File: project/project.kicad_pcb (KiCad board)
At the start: 2 copper layers, 85.5 x 85.5 mm, 53 parts, among them J101 IN, J102 1x7_5.08, J103 1x7_5.08, J104 1x7_5.08, J105 FFC Connector, K1001 P6D-04P, K1101 P6D-04P, K1201 P6D-04P, K1301 P6D-04P, K1401 P6D-04P, K1501 P6D-04P, K1601 P6D-04P, K201 P6D-04P, K301 P6D-04P, K401 P6D-04P, K501 P6D-04P, K601 P6D-04P, K701 P6D-04P, K801 P6D-04P, K901 P6D-04P, U101 GX101

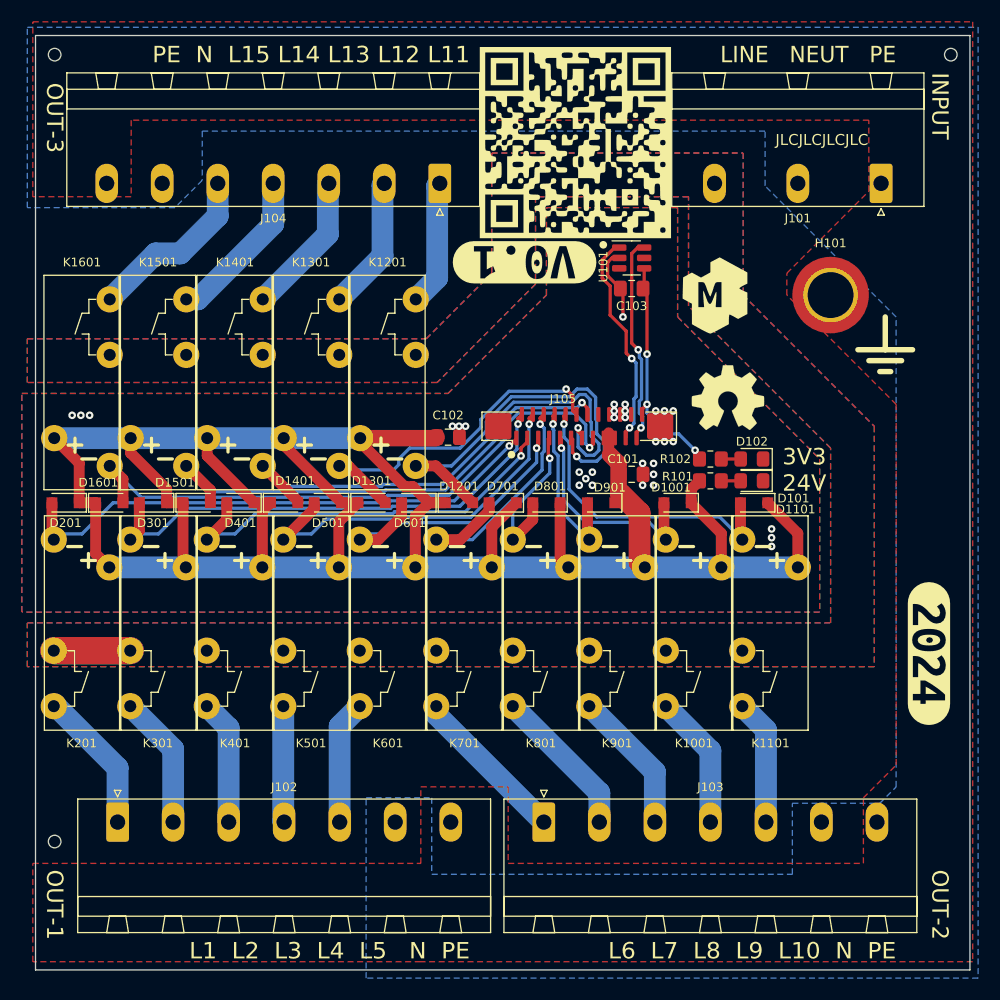
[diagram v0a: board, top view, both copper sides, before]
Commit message: pcb resize, 3d models, inset connectors, gerbers format
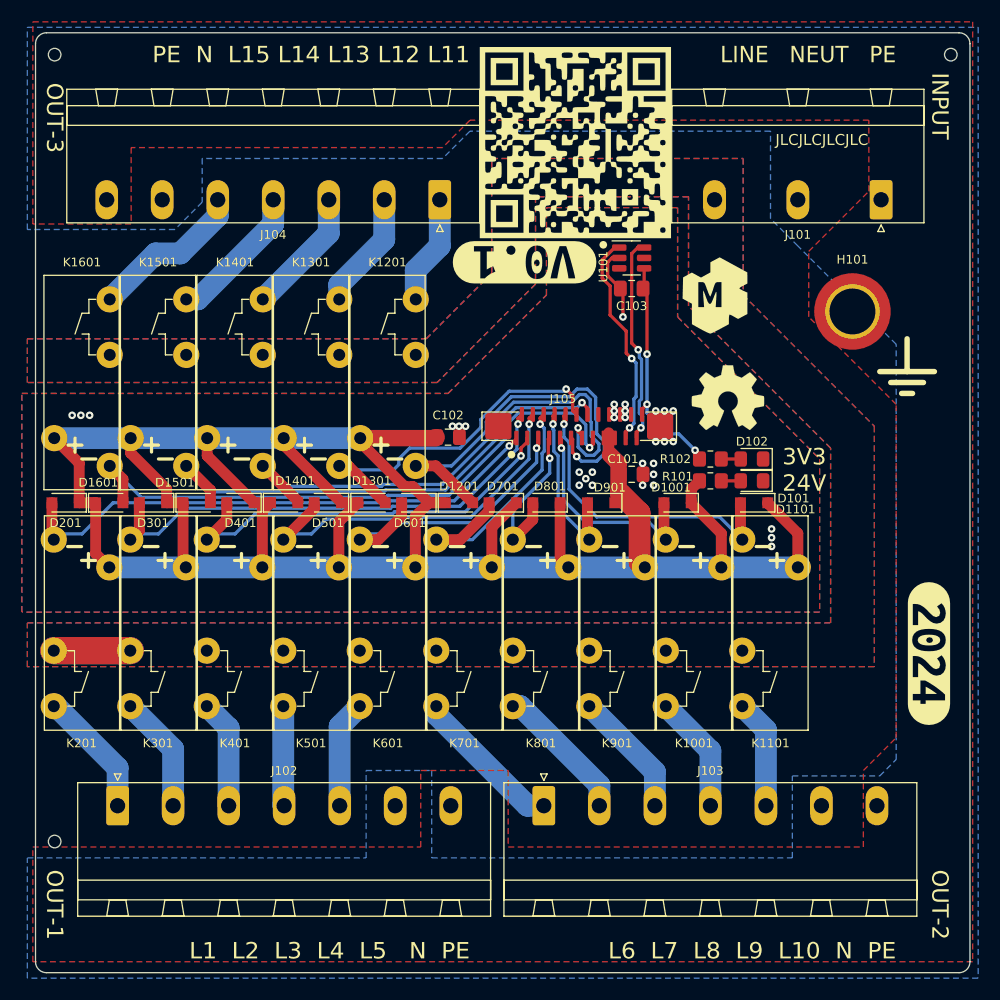
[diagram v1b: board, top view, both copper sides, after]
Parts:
- moved H101 2.50 mm to (200.3, 73.5)
- moved J101 1.50 mm to (202.9, 63.3)
- moved J102 1.50 mm to (133.0, 118.8)
- moved J103 1.50 mm to (172.0, 118.8)
- moved J104 1.50 mm to (162.5, 63.3)
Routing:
- net /_relay8/COM: track 13.9 -> 11.6 mm
- net /_relay13/COM: track 12.3 -> 10.8 mm
- net /_relay12/COM: track 11.5 -> 10.0 mm
- net /_relay9/COM: track 13.1 -> 11.6 mm
- net /_relay6/COM: track 11.4 -> 9.87 mm
- net /_relay5/COM: track 10.6 -> 9.14 mm
- net /_relay4/COM: track 11.4 -> 9.94 mm
- net /_relay3/COM: track 12.2 -> 10.7 mm
- net /_relay2/COM: track 13.1 -> 11.6 mm
- net /_relay16/COM: track 16.0 -> 14.5 mm
- net /_relay15/COM: track 14.5 -> 13.0 mm
- net /_relay11/COM: track 11.5 -> 10.0 mm
- net /_relay10/COM: track 12.3 -> 10.8 mm
- net /_relay14/COM: track 13.1 -> 11.6 mm
- net /_relay7/COM: track 14.7 -> 14.1 mm
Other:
- board size 85.5 x 85.5 mm -> 85.5 x 86 mm

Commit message: bumping up version to v0.2
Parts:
- removed kibuzzard-66DA8205: G***, kibuzzard-66DA8205
- removed kibuzzard-6750110D: G***, kibuzzard-6750110D
- added kibuzzard-6798B3BB: G***, kibuzzard-6798B3BB, F.Cu at (169.3, 69.0)
- added kibuzzard-6798B3C4: G***, kibuzzard-6798B3C4, F.Cu at (207.3, 104.8)

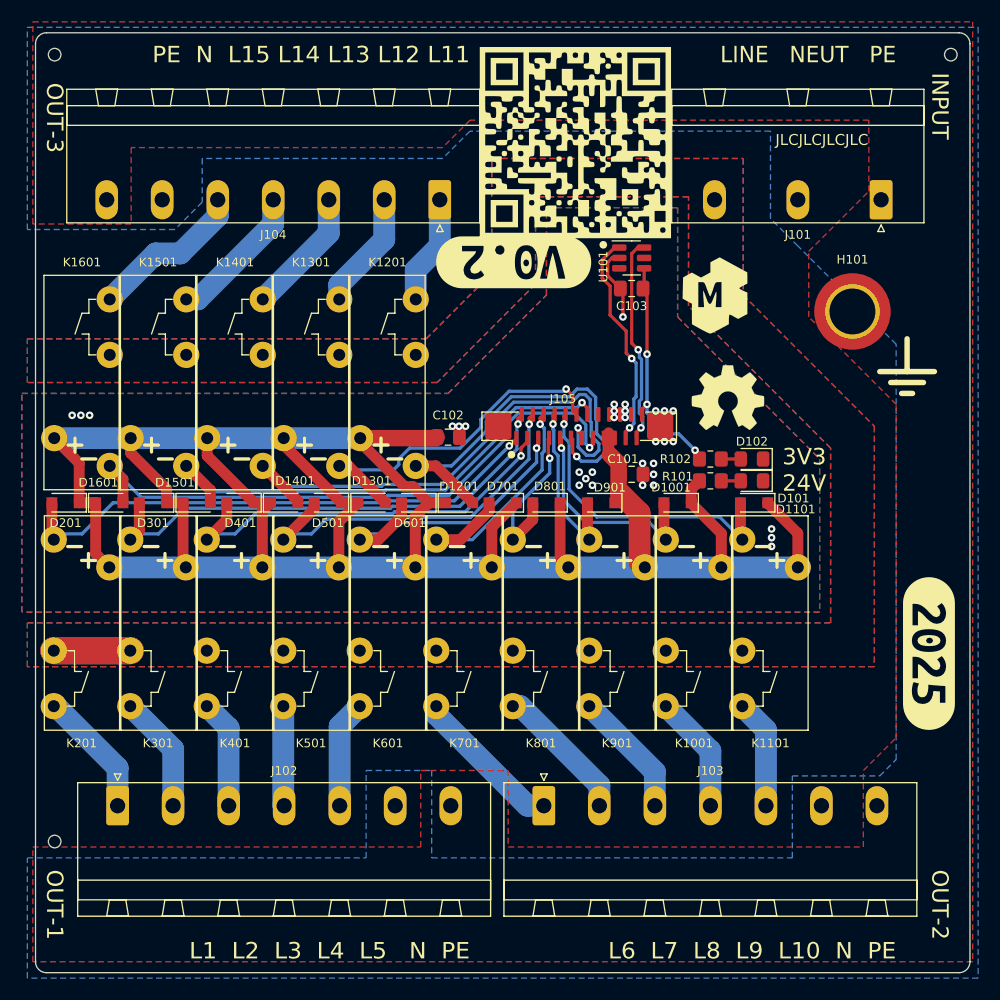
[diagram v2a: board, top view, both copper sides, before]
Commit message: replacing FFC connector
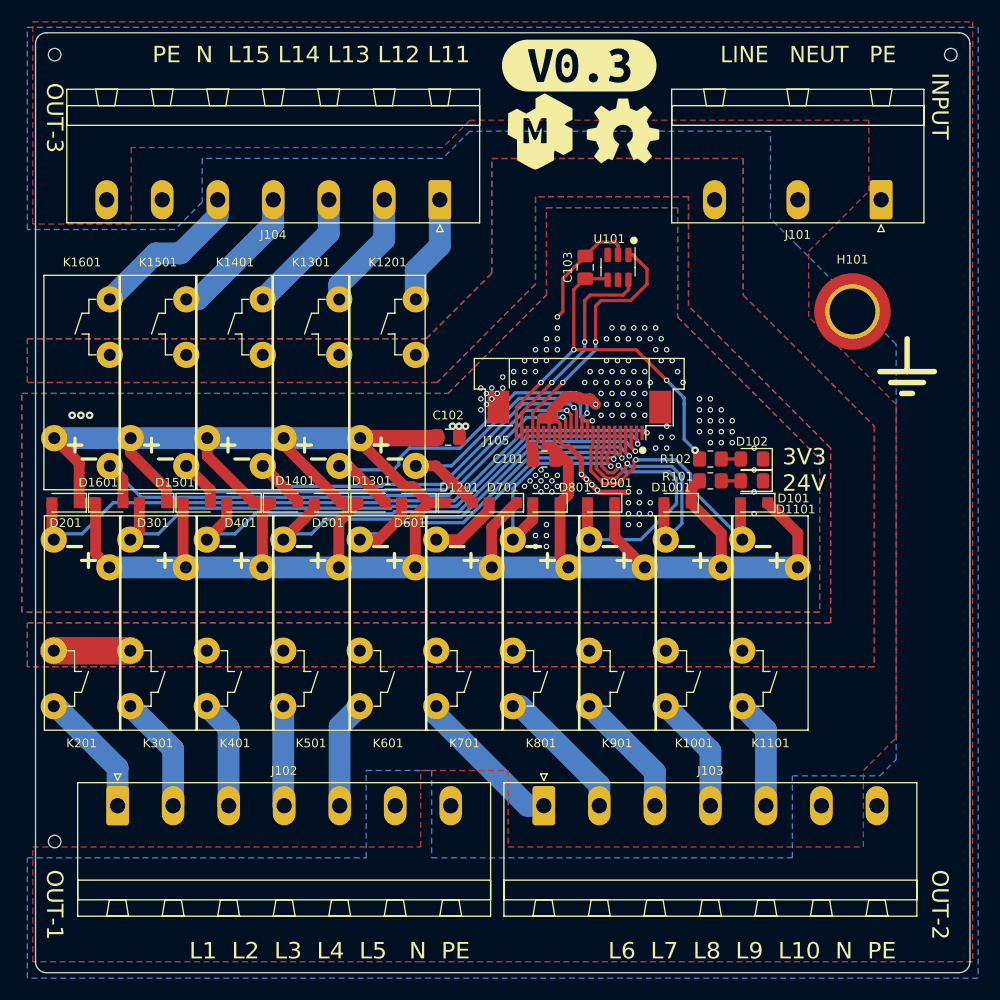
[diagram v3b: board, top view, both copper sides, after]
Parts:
- removed kibuzzard-6798B3BB: G***, kibuzzard-6798B3BB
- added kibuzzard-68EEE57B: G***, kibuzzard-68EEE57B, F.Cu at (175.3, 51.0)
- G***, kibuzzard-6798B3C4: moved to B.Cu
- J105: footprint -local:AFC11-S24ICC-00 -> -local:AFC07-S24FCC-00
- moved kibuzzard-6798B3C4 54.8 mm to (174.3, 61.0), turned to 180 degrees
- moved G*** 38.5 mm to (201.3, 86.0), turned to 180 degrees
- moved G101 26.2 mm to (179.3, 57.0)
- moved G102 21.9 mm to (171.3, 57.0)
- moved C101 8.12 mm to (172.1, 87.0), turned to 180 degrees
- moved C103 4.67 mm to (175.8, 69.5), turned to 90 degrees
- moved U101 1.52 mm to (178.8, 69.5), turned to -90 degrees
- moved J105 0.50 mm to (175.3, 83.5), turned to 180 degrees
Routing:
- net GND: track 6.81 -> 36.3 mm, vias 32 -> 136
- net +3V3: track 21.5 -> 37.1 mm, vias 3 -> 4
- net /_relay2/EN: track 49.7 -> 62.4 mm
- net /_relay4/EN: track 37.9 -> 49.3 mm
- net /_relay14/EN: track 49.9 -> 39.6 mm
- net /_relay9/EN: track 16.3 -> 26.4 mm
- net /_relay3/EN: track 45.9 -> 55.6 mm
- net /_relay12/EN: track 37.2 -> 28.3 mm
- net /_relay6/EN: track 27.4 -> 35.8 mm
- net /_relay5/EN: track 34.3 -> 42.3 mm
- net /_relay8/EN: track 14.9 -> 22.1 mm
- net /_relay16/EN: track 56.2 -> 51.1 mm
- net /_relay7/EN: track 24.4 -> 28.5 mm
- net SCL: track 20.0 -> 23.1 mm
- net +24V: track 219.3 -> 222.4 mm
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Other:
- board text removed: "JLCJLCJLCJLC"
